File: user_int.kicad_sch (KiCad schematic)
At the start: 0 parts

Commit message: finished user interface schematic
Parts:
- added C21: 0.1u, symbol Device:C
- added C22: 1u, symbol Device:C
- added J4: Conn_01x04_Pin, symbol Connector:Conn_01x04_Pin
- added J5: Conn_01x05_Pin, symbol Connector:Conn_01x05_Pin
- added Q2, Q3: BC817, Package_TO_SOT_SMD:SOT-23, symbol Transistor_BJT:BC817
- added R32, R33, R34: 10k, symbol Device:R
- added S1: Boot Button, USLPT2819DT2TR:SW_USLPT2819DT2TR, symbol USLPT2819DT2TR:USLPT2819DT2TR
- added S2: Reset Button, USLPT2819DT2TR:SW_USLPT2819DT2TR, symbol USLPT2819DT2TR:USLPT2819DT2TR
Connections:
- new net: Q3.1 (B), R34.2
- new net: Q2.1 (B), R33.2
- new net +3.3V: J4.1 (Pin_1), J5.1 (Pin_1), R32.2
- new net BOOT: C21.1, Q3.2 (E), S1.3, S1.4
- new net DTR: Q3.3 (C), R33.1
- new net EN: C22.1, Q2.3 (C), R32.1, S2.3
- new net GND: C21.2, C22.2, J4.4 (Pin_4), J5.5 (Pin_5), S1.1, S1.2, S2.1, S2.2
- new net GPIO18: J5.3 (Pin_3)
- new net GPIO19: J5.4 (Pin_4)
- new net GPIO8: J5.2 (Pin_2)
- new net RTS: Q2.2 (E), R34.1
- new net SCL: J4.3 (Pin_3)
- new net SDA: J4.2 (Pin_2)
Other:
- note added: "Breakout for Remaining Pins"
- note added: "OLED Display Connector (I2C)"
- note added: "Reset and BOOT Buttons"

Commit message: setup net classes and started layout
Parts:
- C21, C22: footprint (none) -> Capacitor_SMD:C_0805_2012Metric
- J4: footprint (none) -> Connector_PinHeader_2.54mm:PinHeader_1x04_P2.54mm_Vertical
- J5: footprint (none) -> Connector_PinHeader_2.54mm:PinHeader_1x05_P2.54mm_Vertical
- R32, R33, R34: footprint (none) -> Resistor_SMD:R_0805_2012Metric
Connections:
- net EN: now also S2.4
- net +3.3V renamed +3V3
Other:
- moved on the sheet: C22

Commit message: imported all footprints into layout
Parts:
- S1, S2: footprint USLPT2819DT2TR:SW_USLPT2819DT2TR -> ESP32_project_Footprints:SW_USLPT2819DT2TR; Availability In Stock -> (none); Package None -> (none); Price None -> (none)
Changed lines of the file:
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@@
 			)
 		)
-		(property "Footprint" "USLPT2819DT2TR:SW_USLPT2819DT2TR"
+		(property "Footprint" "ESP32_project_Footprints:SW_USLPT2819DT2TR"
 			(at 219.71 64.77 0)
 			(hide yes)
@@
 			)
 		)
-		(property "Package" "None"
-			(at 219.71 64.77 0)
-			(hide yes)
-			(show_name no)
-			(do_not_autoplace no)
-			(effects
-				(font
-					(size 1.27 1.27)
-				)
-				(justify bottom)
-			)
-		)
-		(property "Price" "None"
-			(at 219.71 64.77 0)
-			(hide yes)
-			(show_name no)
-			(do_not_autoplace no)
-			(effects
-				(font
-					(size 1.27 1.27)
-				)
-				(justify bottom)
-			)
-		)
 		(property "Check_prices" "https://www.snapeda.com/parts/USLPT2819DT2TR/TE+Connectivity+ALCOSWITCH+Switches/view-part/?ref=eda"
 			(at 219.71 64.77 0)
@@
 		)
 		(property "MP" "USLPT2819DT2TR"
-			(at 219.71 64.77 0)
-			(hide yes)
-			(show_name no)
-			(do_not_autoplace no)
-			(effects
-				(font
-					(size 1.27 1.27)
-				)
-				(justify bottom)
-			)
-		)
-		(property "Availability" "In Stock"
 			(at 219.71 64.77 0)
 			(hide yes)
@@
 			)
 		)
-		(property "Footprint" "USLPT2819DT2TR:SW_USLPT2819DT2TR"
+		(property "Footprint" "ESP32_project_Footprints:SW_USLPT2819DT2TR"
 			(at 143.51 62.23 0)
 			(hide yes)
@@
 			)
 		)
-		(property "Package" "None"
-			(at 143.51 62.23 0)
-			(hide yes)
-			(show_name no)
-			(do_not_autoplace no)
-			(effects
-				(font
-					(size 1.27 1.27)
-				)
-				(justify bottom)
-			)
-		)
-		(property "Price" "None"
-			(at 143.51 62.23 0)
-			(hide yes)
-			(show_name no)
-			(do_not_autoplace no)
-			(effects
-				(font
-					(size 1.27 1.27)
-				)
-				(justify bottom)
-			)
-		)
 		(property "Check_prices" "https://www.snapeda.com/parts/USLPT2819DT2TR/TE+Connectivity+ALCOSWITCH+Switches/view-part/?ref=eda"
 			(at 143.51 62.23 0)
@@
 			(at 143.51 62.23 0)
 			(hide yes)
-			(show_name no)
-			(do_not_autoplace no)
-			(effects
-				(font
-					(size 1.27 1.27)
-				)
-				(justify bottom)
-			)
-		)
-		(property "Availability" "In Stock"
-			(at 143.51 62.23 0)
-			(hide yes)

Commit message: corrected boot control schematic and layout
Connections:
- net BOOT: now also Q3.3 (C); no longer Q3.2 (E)
- net DTR: now also Q3.2 (E); no longer Q3.3 (C)
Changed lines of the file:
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@@
-	(wire
-		(pts
-			(xy 170.18 119.38) (xy 170.18 115.57)
-		)
-		(stroke
-			(width 0)
-			(type default)
-		)
-	)
 	(wire
 		(pts
@@
 	(wire
 		(pts
+			(xy 148.59 124.46) (xy 162.56 124.46)
+		)
+		(stroke
+			(width 0)
+			(type default)
+		)
+	)
+	(wire
+		(pts
 			(xy 128.27 124.46) (xy 135.89 124.46)
 		)
@@
 	(wire
 		(pts
+			(xy 52.07 113.03) (xy 43.18 113.03)
+		)
+		(stroke
+			(width 0)
+			(type default)
+		)
+	)
+	(wire
+		(pts
+			(xy 41.91 66.04) (xy 46.99 66.04)
+		)
+		(stroke
+			(width 0)
+			(type default)
+		)
+	)
+	(wire
+		(pts
+			(xy 41.91 63.5) (xy 46.99 63.5)
+		)
+		(stroke
+			(width 0)
+			(type default)
+		)
+	)
+	(wire
+		(pts
+			(xy 205.74 67.31) (xy 205.74 71.12)
+		)
+		(stroke
+			(width 0)
+			(type default)
+		)
+	)
+	(wire
+		(pts
+			(xy 229.87 52.07) (xy 229.87 62.23)
+		)
+		(stroke
+			(width 0)
+			(type default)
+		)
+	)
+	(wire
+		(pts
+			(xy 128.27 64.77) (xy 128.27 69.85)
+		)
+		(stroke
+			(width 0)
+			(type default)
+		)
+	)
+	(wire
+		(pts
+			(xy 41.91 69.85) (xy 41.91 66.04)
+		)
+		(stroke
+			(width 0)
+			(type default)
+		)
+	)
+	(wire
+		(pts
+			(xy 170.18 115.57) (xy 170.18 119.38)
+		)
+		(stroke
+			(width 0)
+			(type default)
+		)
+	)
+	(wire
+		(pts
+			(xy 205.74 67.31) (xy 212.09 67.31)
+		)
+		(stroke
+			(width 0)
+			(type default)
+		)
+	)
+	(wire
+		(pts
+			(xy 212.09 62.23) (xy 209.55 62.23)
+		)
+		(stroke
+			(width 0)
+			(type default)
+		)
+	)
+	(wire
+		(pts
+			(xy 205.74 80.01) (xy 205.74 82.55)
+		)
+		(stroke
+			(width 0)
+			(type default)
+		)
+	)
+	(wire
+		(pts
 			(xy 170.18 129.54) (xy 170.18 138.43)
 		)
@@
 	(wire
 		(pts
-			(xy 52.07 113.03) (xy 43.18 113.03)
-		)
-		(stroke
-			(width 0)
-			(type default)
-		)
-	)
-	(wire
-		(pts
-			(xy 41.91 66.04) (xy 46.99 66.04)
-		)
-		(stroke
-			(width 0)
-			(type default)
-		)
-	)
-	(wire
-		(pts
-			(xy 41.91 63.5) (xy 46.99 63.5)
-		)
-		(stroke
-			(width 0)
-			(type default)
-		)
-	)
-	(wire
-		(pts
-			(xy 205.74 67.31) (xy 205.74 71.12)
-		)
-		(stroke
-			(width 0)
-			(type default)
-		)
-	)
-	(wire
-		(pts
-			(xy 229.87 52.07) (xy 229.87 62.23)
-		)
-		(stroke
-			(width 0)
-			(type default)
-		)
-	)
-	(wire
-		(pts
-			(xy 128.27 64.77) (xy 128.27 69.85)
-		)
-		(stroke
-			(width 0)
-			(type default)
-		)
-	)
-	(wire
-		(pts
-			(xy 41.91 69.85) (xy 41.91 66.04)
-		)
-		(stroke
-			(width 0)
-			(type default)
-		)
-	)
-	(wire
-		(pts
-			(xy 205.74 67.31) (xy 212.09 67.31)
-		)
-		(stroke
-			(width 0)
-			(type default)
-		)
-	)
-	(wire
-		(pts
-			(xy 212.09 62.23) (xy 209.55 62.23)
-		)
-		(stroke
-			(width 0)
-			(type default)
-		)
-	)
-	(wire
-		(pts
-			(xy 205.74 80.01) (xy 205.74 82.55)
-		)
-		(stroke
-			(width 0)
-			(type default)
-		)
-	)
-	(wire
-		(pts
 			(xy 209.55 52.07) (xy 229.87 52.07)
-		)
-		(stroke
-			(width 0)
-			(type default)
-		)
-	)
-	(wire
-		(pts
-			(xy 148.59 124.46) (xy 162.56 124.46)
 		)
 		(stroke
@@
 		(lib_id "Transistor_BJT:BC817")
 		(at 167.64 124.46 0)
+		(mirror x)
 		(unit 1)
 		(body_style 1)
@@
 		(in_pos_files yes)
 		(dnp no)
-		(fields_autoplaced yes)
 		(property "Reference" "Q3"
-			(at 172.72 123.1899 0)
+			(at 172.72 125.7301 0)
 			(show_name no)
 			(do_not_autoplace no)
@@
 		)
 		(property "Value" "BC817"
-			(at 172.72 125.7299 0)
+			(at 172.72 123.1901 0)
 			(show_name no)
 			(do_not_autoplace no)
@@
 		)
 		(property "Footprint" "Package_TO_SOT_SMD:SOT-23"
-			(at 172.72 126.365 0)
-			(hide yes)
-			(show_name no)
+			(at 172.72 122.555 0)
+			(hide yes)
+			(show_name no)

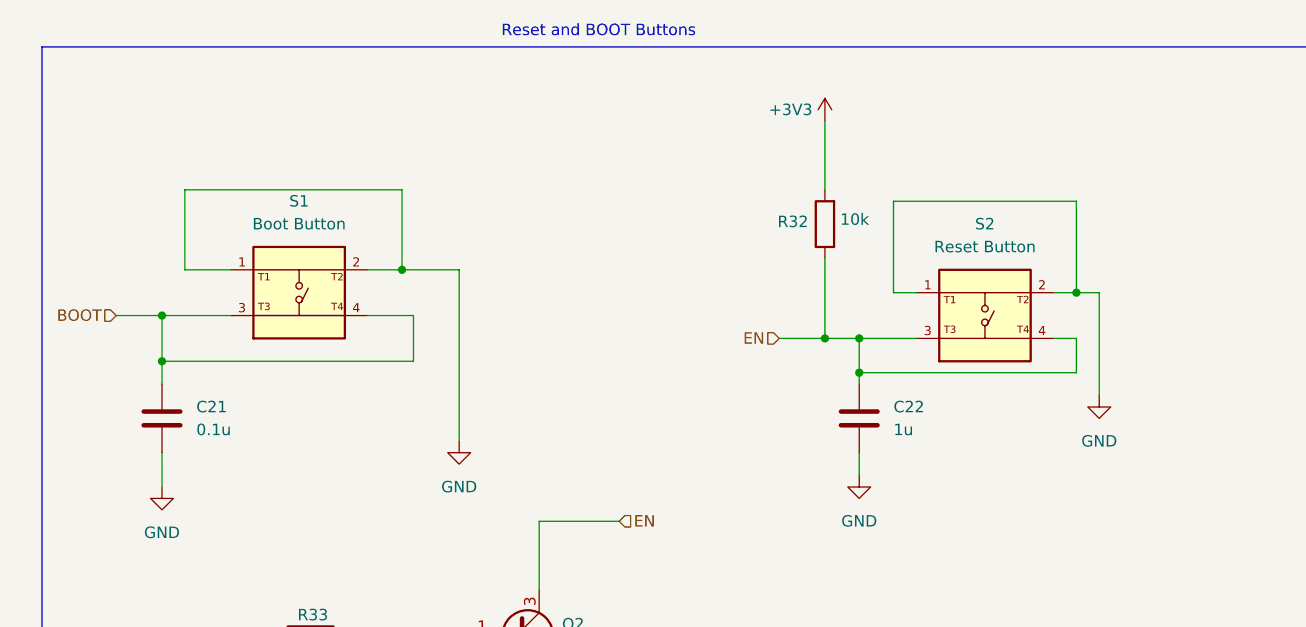
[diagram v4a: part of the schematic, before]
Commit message: added pot to mic amp, made buttons bigger
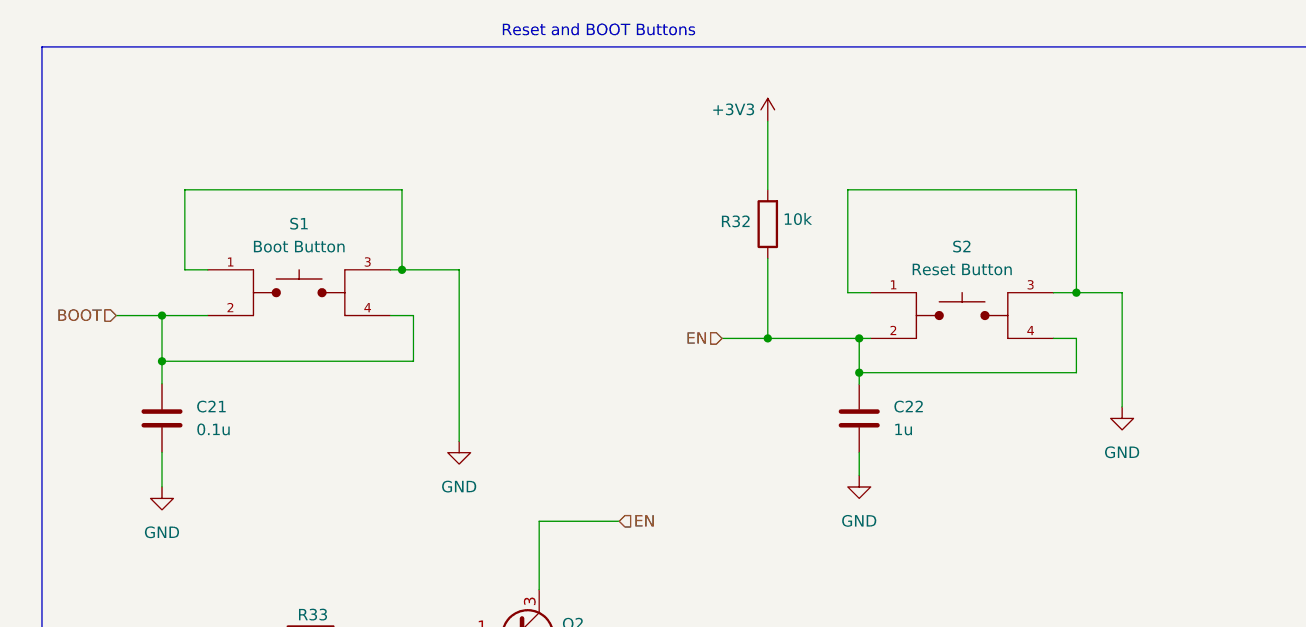
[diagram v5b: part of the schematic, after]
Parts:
- S1, S2: footprint ESP32_project_Footprints:SW_USLPT2819DT2TR -> ESP32_project_Footprints:SW_TL3305AF260QG; symbol USLPT2819DT2TR:USLPT2819DT2TR -> TL3305AF260QG:TL3305AF260QG; Availability (none) -> In Stock; Check_prices https://www.snapeda.com/parts/USLPT2819DT2TR/TE+Connectivit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 -> https://www.snapeda.com/parts/TL3305AF260QG/E-Switch/view-p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; MANUFACTURER TE CONNECTIVITY -> E-Switch; MAXIMUM_PACKAGE_HEIGHT (none) -> 3.8mm; MF TE Connectivity -> E-Switch; MP USLPT2819DT2TR -> TL3305AF260QG; PARTREV P -> C; Package (none) -> SMD-4 E-Switch; Price (none) -> None; STANDARD Manufacturer Recommendations -> Manufacturer recommendations; SnapEDA_Link https://www.snapeda.com/parts/USLPT2819DT2TR/TE+Connectivit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 -> https://www.snapeda.com/parts/TL3305AF260QG/E-Switch/view-p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
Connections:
- net BOOT: now also S1.2; no longer S1.3
- net EN: now also S2.2; no longer S2.3
- net GND: now also S1.3, S2.3; no longer S1.2, S2.2
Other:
- moved on the sheet: R32
